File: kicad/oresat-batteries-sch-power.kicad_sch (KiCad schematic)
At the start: 88 parts, among them Q1 MOSFET-PCH-SOT23-6, Q2 PMV45EN, Q3 MOSFET-PCH-SOT23-6, Q4 MOSFET-PCH-SOT23-6, Q44 PMV45EN, Q5 PMV45EN, U1 MAX7310, U2 MIC842LYC5, U3 MIC842LYC5, U4 MAX4211, U5 TPS6211X, U6 TS5A21366DCUR

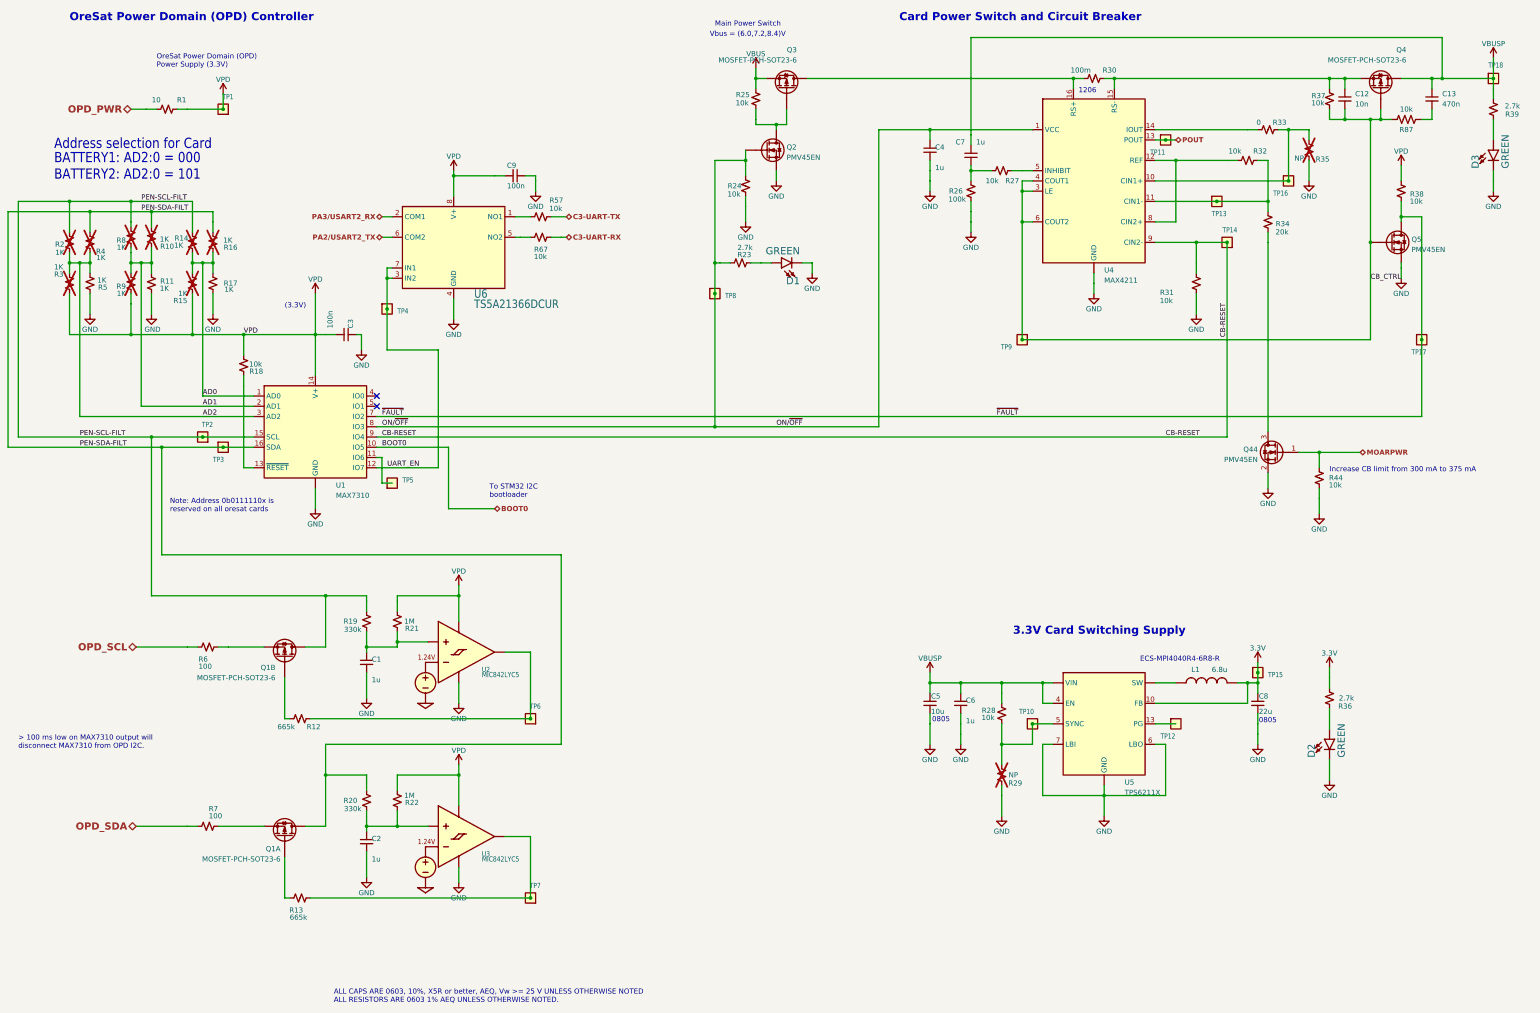
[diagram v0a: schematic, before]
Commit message: Progress on battery card v4
Moved in -batt cutoffs, which caused a lot of pain and suffering. Started updating BOM, and fixed all transistor packages. Updated resistor packages, too. Still needs a lot of cleanup, but probably 80% done now.
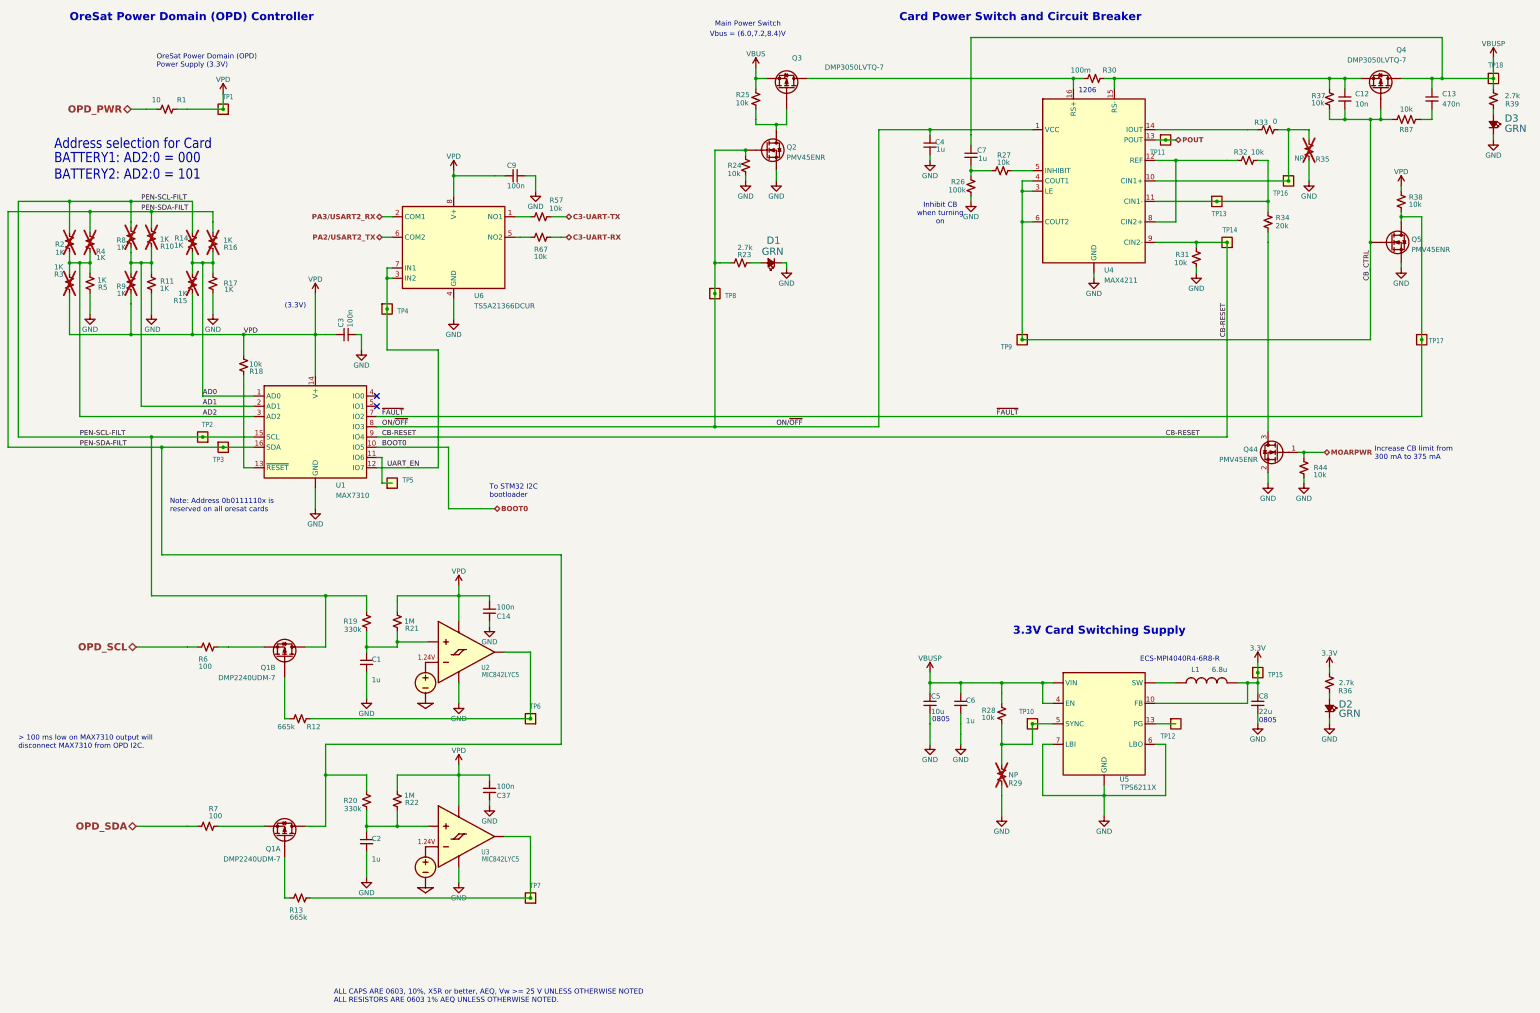
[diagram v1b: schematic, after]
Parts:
- added C14, C37: 100n, oresat-passives:0603-C-NOSILK, symbol Device:C_Small
- C1, C12, C13, C2, C3, C4, C6, C7, C9: footprint oresat-passives:c_0603-SMALL -> oresat-passives:0603-C-NOSILK
- C5, C8: footprint oresat-passives:0805-B-NOSILK -> oresat-passives:0805-C-NOSILK
- D1, D2, D3: value GREEN -> GRN; footprint oresat-batteries:LED-0603 -> LED_SMD:LED_0603_1608Metric; symbol oresat-batteries-eagle-import:LED-GREEN0603 -> Device:LED_Small_Filled
- Q1: value MOSFET-PCH-SOT23-6 -> DMP2240UDM-7; footprint oresat-batteries:SOT23-6 -> Package_TO_SOT_SMD:SOT-23-6; DIS Digi-Key -> DigiKey; DPN GRM21BR61A226ME51L -> DMP2240UDMDICT-ND; MFR Diodes Inc -> Diodes Incorporated; MPN DMP2240UDM -> DMP2240UDM-7
- Q2, Q44, Q5: value PMV45EN -> PMV45ENR; footprint oresat-batteries:SOT23-3 -> Package_TO_SOT_SMD:SOT-23; DIS Digi-Key -> DigiKey
- Q3, Q4: value MOSFET-PCH-SOT23-6 -> DMP3050LVTQ-7; DIS Digi-Key -> DigiKey; DPN DMP3050LVT-7DICT-ND -> 31-DMP3050LVTQ-7-ND; MPN DMP3050LVT-7 -> DMP3050LVTQ-7
- R1, R11, R12, R13, R17, R5, R6, R7: footprint oresat-batteries:.0603-C-NOSILK -> oresat-passives:0603-C-NOSILK; DIS Digi-Key -> DigiKey
- R18, R19, R20, R21, R22, R23, R24, R25, R26, R27, R28, R31, R32, R33, R34, R36, R37, R38, R39, R44, R57, R67: footprint oresat-batteries:.0603-C-NOSILK -> oresat-passives:0603-C-NOSILK
- R30: footprint oresat-batteries:1206-C -> oresat-passives:1206-C
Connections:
- net GND: now also D1.1 (K), D2.1 (K), D3.1 (K), C14.2, C37.2; no longer D1.C, D2.C, D3.C
- net VPD: now also C14.1, C37.1
- net at R39.1: now also D3.2 (A); no longer D3.A
- net at R23.1: now also D1.2 (A); no longer D1.A
- net at R36.1: now also D2.2 (A); no longer D2.A
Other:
- note added: "Inhibit CB when turning on"
- moved on the sheet: C4, R24, R26, R31, R36, R38, R39, R44

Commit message: Routing complete!
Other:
- moved on the sheet: TP5
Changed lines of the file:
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@@
 	(text "To STM32 I2C\nbootloader"
 		(exclude_from_sim no)
-		(at 151.13 140.97 0)
+		(at 156.21 130.302 0)
 		(effects
 			(font
@@
 	(wire
 		(pts
-			(xy 140.97 143.51) (xy 152.4 143.51)
-		)
-		(stroke
-			(width 0.1524)
-			(type solid)
-		)
-	)
-	(wire
-		(pts
 			(xy 52.07 80.01) (xy 52.07 82.55)
 		)
@@
 	(wire
 		(pts
-			(xy 107.95 138.43) (xy 107.95 143.51)
+			(xy 107.95 138.43) (xy 107.95 139.7)
 		)
 		(stroke
@@
 	(wire
 		(pts
-			(xy 123.19 128.27) (xy 140.97 128.27)
+			(xy 123.19 128.27) (xy 147.32 128.27)
 		)
 		(stroke
@@
 	(wire
 		(pts
-			(xy 140.97 128.27) (xy 140.97 143.51)
-		)
-		(stroke
-			(width 0.1524)
-			(type solid)
-		)
-	)
-	(wire
-		(pts
 			(xy 346.71 49.53) (xy 349.25 49.53)
 		)
@@
 	(wire
 		(pts
-			(xy 142.24 91.44) (xy 142.24 96.52)
+			(xy 142.24 91.44) (xy 142.24 93.98)
 		)
 		(stroke
@@
 	(wire
 		(pts
-			(xy 124.46 137.16) (xy 127 137.16)
+			(xy 124.46 137.16) (xy 128.27 137.16)
 		)
 		(stroke
@@
 	)
 	(label "AD1"
-		(at 80.01 118.11 0)
+		(at 85.09 118.11 0)
 		(effects
 			(font
@@
 	)
 	(label "AD0"
-		(at 80.01 115.57 0)
+		(at 85.09 115.57 0)
 		(effects
 			(font
@@
 	)
 	(label "AD2"
-		(at 80.01 120.65 0)
+		(at 85.09 120.65 0)
 		(effects
 			(font
@@
 	(hierarchical_label "BOOT0"
 		(shape bidirectional)
-		(at 152.4 143.51 0)
+		(at 147.32 128.27 0)
 		(effects
 			(font
@@
 		(dnp no)
 		(property "Reference" "TP3"
-			(at 82.55 132.08 0)
+			(at 83.566 131.318 0)
 			(effects
 				(font
@@
 		(dnp no)
 		(property "Reference" "TP2"
-			(at 82.55 121.92 0)
+			(at 81.788 122.682 0)
 			(effects
 				(font
@@
 	(symbol
 		(lib_id "power:GND")
-		(at 142.24 96.52 0)
+		(at 142.24 93.98 0)
 		(mirror y)
 		(unit 1)
@@
 		(dnp no)
 		(property "Reference" "#PWR34"
-			(at 142.24 102.87 0)
+			(at 142.24 100.33 0)
 			(effects
 				(font
@@
 		)
 		(property "Value" "GND"
-			(at 142.24 100.33 0)
+			(at 142.24 97.79 0)
 			(effects
 				(font
@@
 		)
 		(property "Footprint" ""
-			(at 142.24 96.52 0)
+			(at 142.24 93.98 0)
 			(effects
 				(font
@@
 		)
 		(property "Datasheet" ""
-			(at 142.24 96.52 0)
+			(at 142.24 93.98 0)
 			(effects
 				(font
@@
 		)
 		(property "Description" "Power symbol creates a global label with name \"GND\" , ground"
-			(at 142.24 96.52 0)
+			(at 142.24 93.98 0)
 			(effects
 				(font
@@
 	(symbol
 		(lib_id "oresat-misc:Test-Point-0.75mm-th")
-		(at 127 137.16 90)
+		(at 128.27 137.16 90)
 		(unit 1)
 		(exclude_from_sim yes)
@@
 		(dnp no)
 		(property "Reference" "TP5"
-			(at 129.54 137.16 90)
+			(at 130.048 137.922 90)
 			(effects
 				(font
@@
 		)
 		(property "Value" "TEST-POINT-LARGE-SQUARE"
-			(at 127 137.16 0)
+			(at 128.27 137.16 0)
 			(effects
 				(font
@@
 		)
 		(property "Footprint" "oresat-misc:TestPoint-0.75mm-th"
-			(at 116.84 137.16 0)
+			(at 118.11 137.16 0)
 			(effects
 				(font
@@
 		)
 		(property "Datasheet" ""
-			(at 127 137.16 0)
+			(at 128.27 137.16 0)
 			(effects
 				(font
@@
 		)
 		(property "Description" "0.75 mm TH test point; good for scope probes and jumpers"
-			(at 127 137.16 0)
+			(at 128.27 137.16 0)
 			(effects
 				(font
@@
 	(symbol
 		(lib_id "power:GND")
-		(at 107.95 143.51 0)
+		(at 107.95 139.7 0)
 		(mirror y)
 		(unit 1)
@@
 		(dnp no)
 		(property "Reference" "#PWR9"
-			(at 107.95 149.86 0)
+			(at 107.95 146.05 0)
 			(effects
 				(font
@@
 		)
 		(property "Value" "GND"
-			(at 107.95 147.32 0)
+			(at 107.95 143.51 0)
 			(effects
 				(font
@@
 		)
 		(property "Footprint" ""
-			(at 107.95 143.51 0)
+			(at 107.95 139.7 0)
 			(effects
 				(font
@@
 		)
 		(property "Datasheet" ""
-			(at 107.95 143.51 0)
+			(at 107.95 139.7 0)
 			(effects
 				(font
@@
 		)
 		(property "Description" "Power symbol creates a global label with name \"GND\" , ground"
-			(at 107.95 143.51 0)
+			(at 107.95 139.7 0)
 			(effects
 				(font

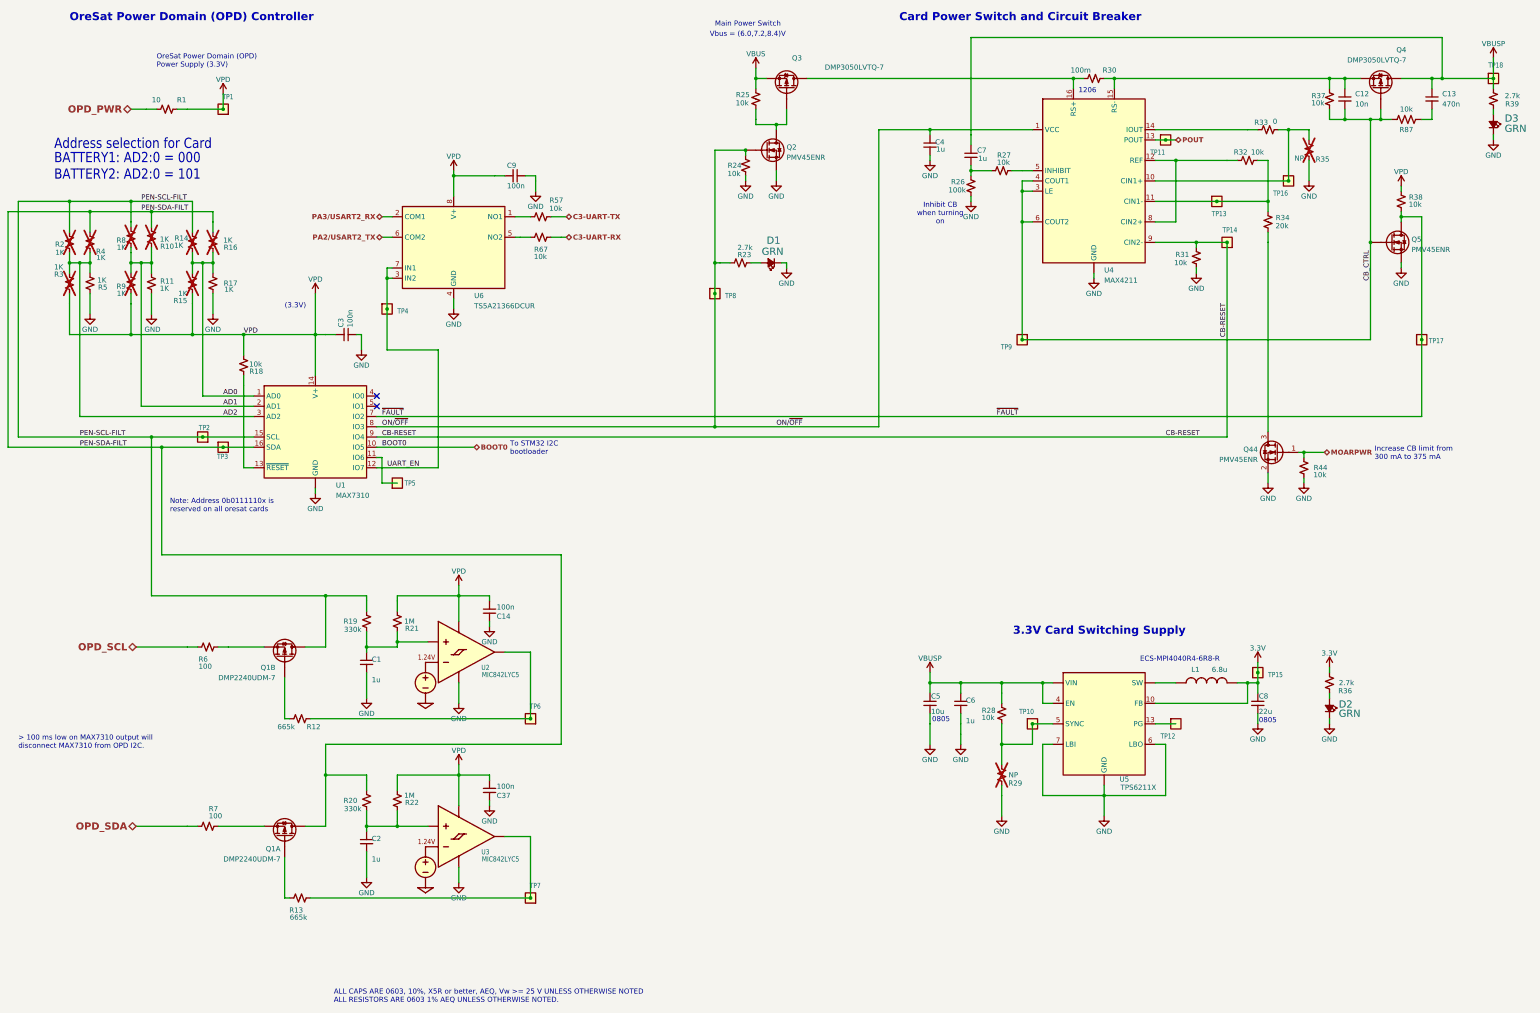
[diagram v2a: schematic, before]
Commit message: Updated BOM, ready for polish and switch to MCXN
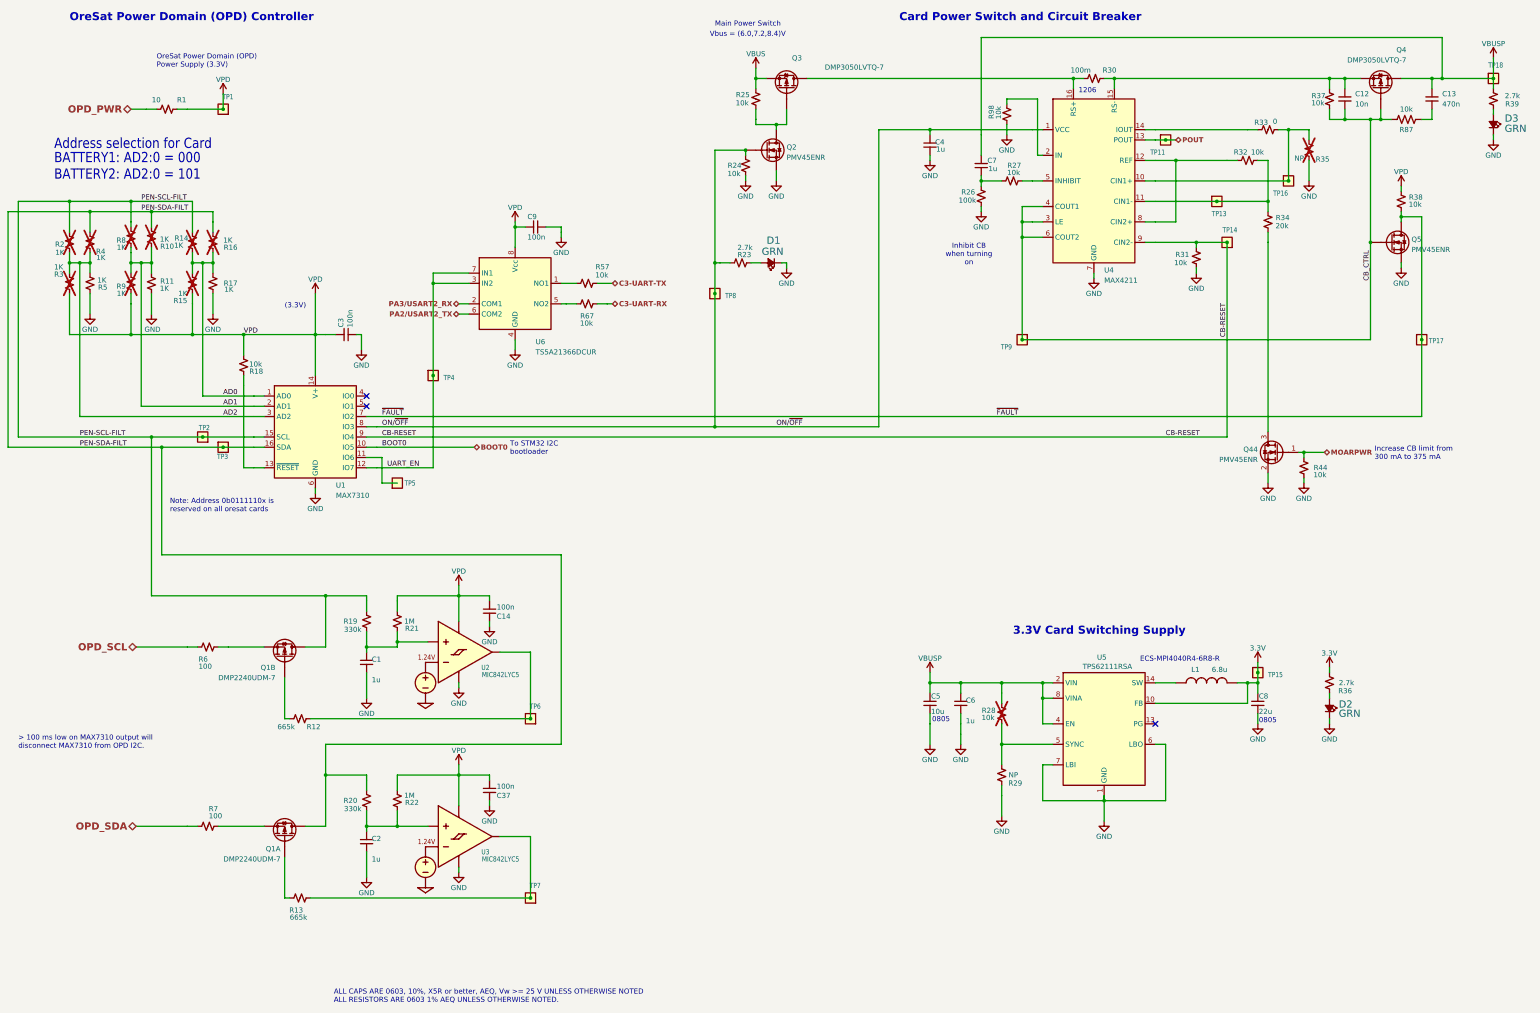
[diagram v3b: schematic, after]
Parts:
- removed TP10, TP12: TEST-POINT-LARGE-SQUARE, oresat-misc:TestPoint-0.75mm-th, symbol oresat-misc:Test-Point-0.75mm-th
- added R98: 10k, oresat-passives:0603-C-NOSILK, symbol Device:R_Small_US
- L1: footprint oresat-batteries:ECS-MPI4040 -> oresat-passives:L_ECS-MPI4040
- R28: now not fitted
- R29: now fitted
- U1: footprint oresat-batteries:QFN65P400X400X80-17T210 -> Package_DFN_QFN:QFN-16-1EP_4x4mm_P0.65mm_EP2.1x2.1mm; symbol oresat-batteries-eagle-import:MAX7310 -> oresat-ics:MAX7310
- U2, U3: footprint oresat-batteries:SC70-5 -> Package_TO_SOT_SMD:SOT-353_SC-70-5; symbol oresat-batteries-eagle-import:MIC842LYC5 -> oresat-ics:MIC842LYC5
- U4: footprint oresat-batteries:QFN65P400X400X80-17T210 -> Package_DFN_QFN:QFN-16-1EP_4x4mm_P0.65mm_EP2.1x2.1mm; symbol oresat-batteries-eagle-import:MAX4211 -> oresat-ics:MAX4211D/E/F
- U5: value TPS6211X -> TPS62111RSA; footprint oresat-batteries:S-PVQFN-16 -> Package_DFN_QFN:Texas_RSA_VQFN-16-1EP_4x4mm_P0.65mm_EP2.7x2.7mm; symbol oresat-batteries-eagle-import:TPS6211X -> oresat-ics:TPS6211X
- U6: footprint oresat-batteries:DCU0008A_N -> Package_SO:VSSOP-8_2.3x2mm_P0.5mm; symbol oresat-batteries-eagle-import:TS5A21366DCUR -> oresat-ics:TS5A21366
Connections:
- net GND: now also U1.17 (GND), U4.17 (GND), U5.17 (GND), R98.2; no longer U1.EPAD (GND), U4.EPAD (GND), U5.PAD (GND)
- new net: R98.1, U4.2 (IN)
- no-connect marks 2 -> 3
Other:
- moved on the sheet: C7, C9, R26, R27, R57, R67, TP4, U2, U3, U6
